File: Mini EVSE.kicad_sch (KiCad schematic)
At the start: 58 parts, among them IC1 74LVC2G04, IC2 IRM-03-5, IC3 ATMEGA328PB-A, IC4 TMR1-0522, IC5 SI8261BAC-C-IP, IC6 BD6211F-E2, IC7 BD6211F-E2, IC8 HCPL3700, IC9 HCPL3700, J10 M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

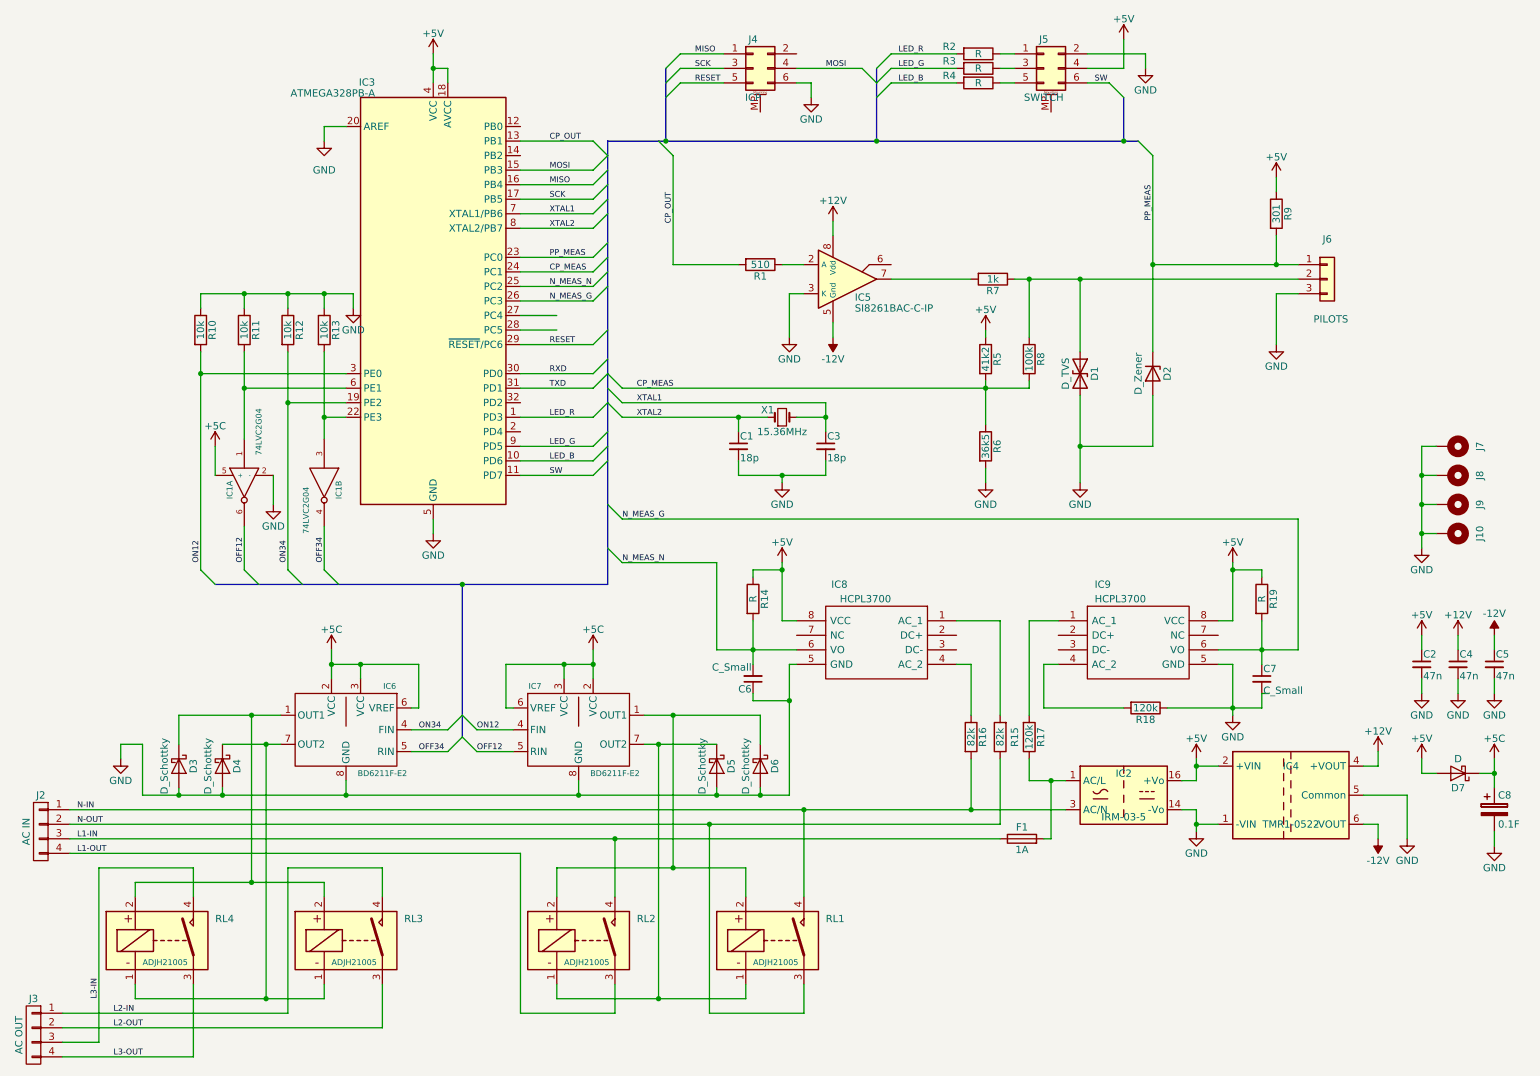
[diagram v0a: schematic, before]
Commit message: Removed need for rescue library
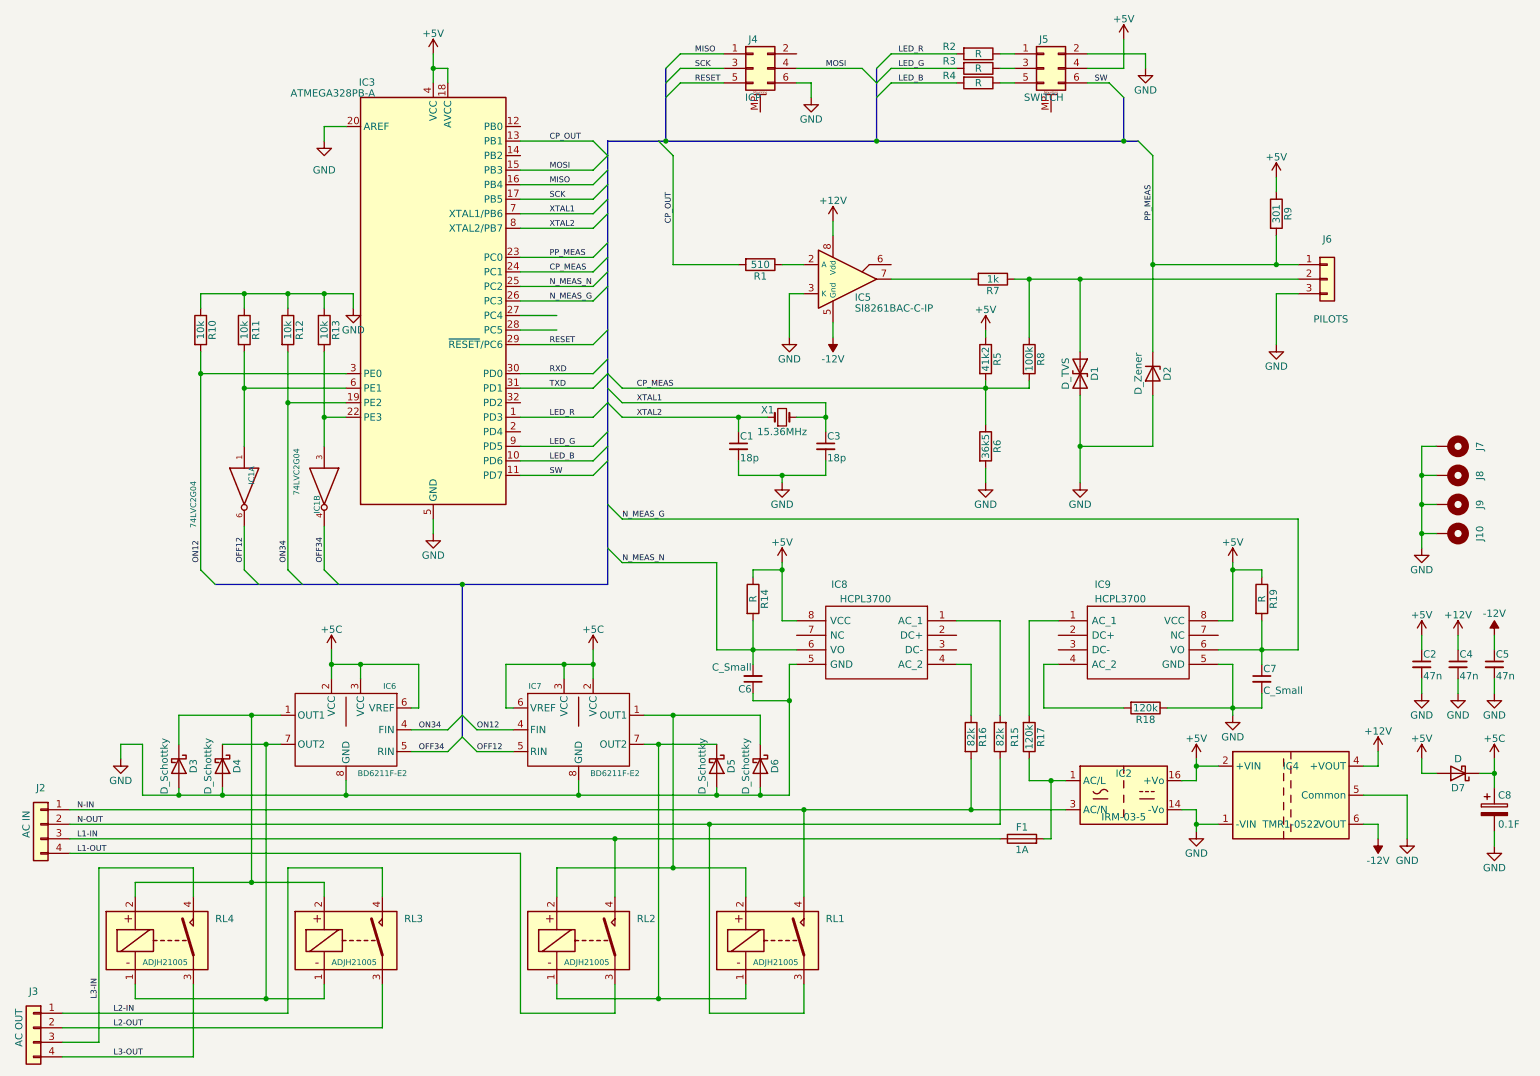
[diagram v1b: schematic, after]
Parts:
- C8: symbol Mini-EVSE-rescue:CP -> Device:C_Polarized
- D3, D4, D5, D6, D7: symbol Mini-EVSE-rescue:D_Schottky -> Device:D_Schottky
- IC1: symbol Mini-EVSE-rescue:74LVC2G04 -> 74xGxx:74LVC2G04
- IC6, IC7: symbol Mini-EVSE-rescue:BD6211F-E2 -> miscellaneous:BD6211F-E2
- IC8, IC9: footprint Housings_DIP:SMDIP-8_W7.62mm -> DIP762W56P254L966H508Q8N; symbol Mini-EVSE-rescue:HCPL3700 -> SamacSys_Parts:HCPL3700
- J2, J3: symbol Mini-EVSE-rescue:CONN_01X04 -> Connector_Generic:Conn_01x04
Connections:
- net +5C: now also IC1.5 (+5C)
- net GND: now also IC1.2 (GND)
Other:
- moved on the sheet: IC1B
